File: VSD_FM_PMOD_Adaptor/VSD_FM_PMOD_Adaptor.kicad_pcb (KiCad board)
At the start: 2 copper layers, 58.2 x 29.8 mm, 22 parts, among them J1 PMOD, J2 PMOD, U1 VSDSquadron FM, U2 AMS1117-3.3

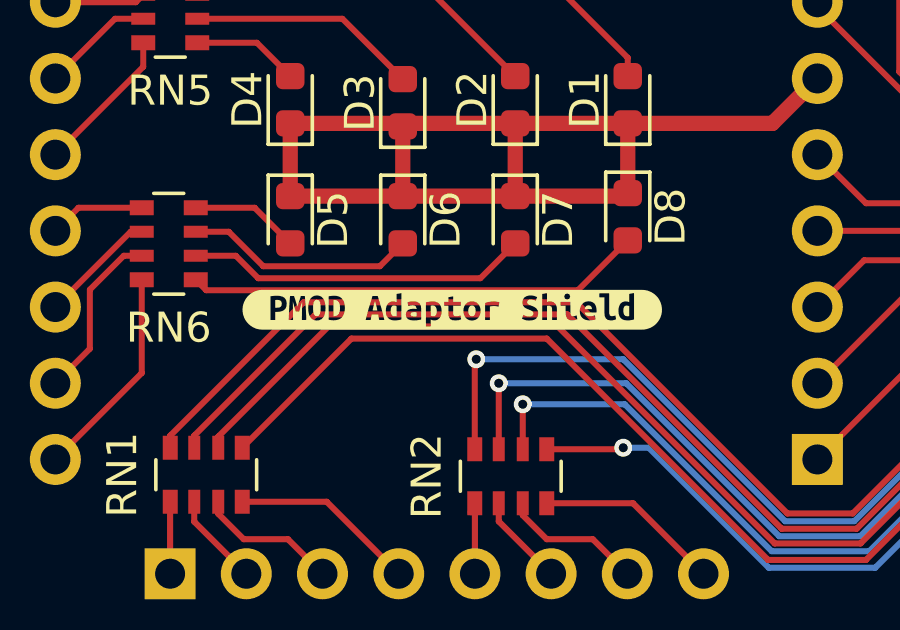
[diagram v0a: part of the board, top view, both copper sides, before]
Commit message: Updated LCSC component part numbers
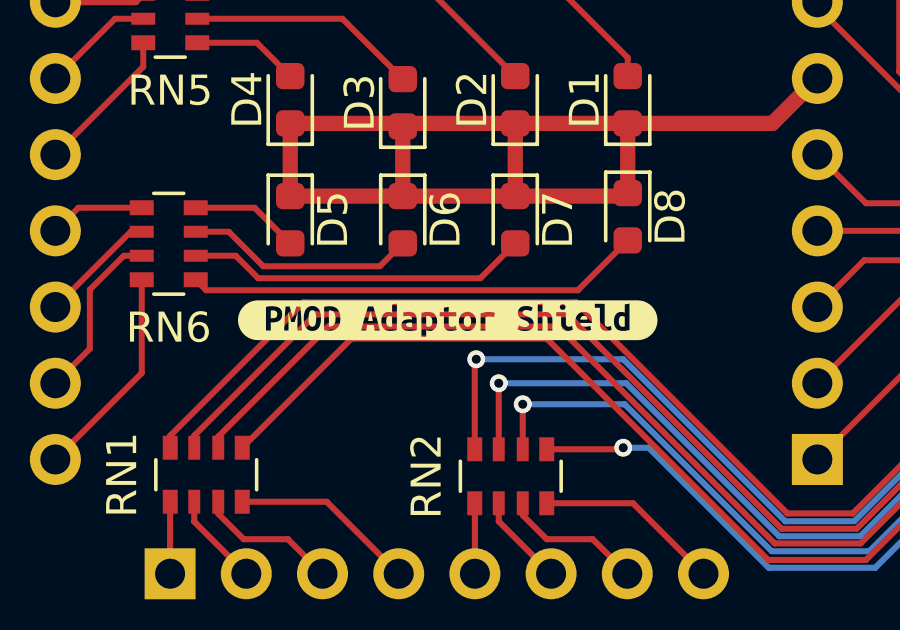
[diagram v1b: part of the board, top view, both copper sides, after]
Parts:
- moved kibuzzard-679249C3 0.38 mm to (126.2, 110.5)
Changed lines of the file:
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@@
 			)
 		)
-		(property "LCSC" ""
+		(property "LCSC" "C965799"
 			(at 0 0 -90)
 			(unlocked yes)
@@
 		(property ki_fp_filters "LED* LED_SMD:* LED_THT:*")
 		(sheetname "Root")
-		(sheetfile "VSD_FM_multi_pmod.kicad_sch")
+		(sheetfile "VSD_FM_PMOD_Adaptor.kicad_sch")
 		(attr smd)
 		(fp_line
@@
 			)
 		)
-		(property "LCSC" ""
+		(property "LCSC" "C965799"
 			(at 0 0 90)
 			(unlocked yes)
@@
 		(property ki_fp_filters "LED* LED_SMD:* LED_THT:*")
 		(sheetname "Root")
-		(sheetfile "VSD_FM_multi_pmod.kicad_sch")
+		(sheetfile "VSD_FM_PMOD_Adaptor.kicad_sch")
 		(attr smd)
 		(fp_line
@@
 	(footprint "kibuzzard-679249C3"
 		(layer "F.Cu")
-		(at 126.4 110.1)
+		(at 126.25 110.45)
 		(descr "Generated with KiBuzzard")
 		(tags "kb_params=eyJBbGlnbm1lbnRDaG9pY2UiOiAiQ2VudGVyIiwgIkNhcExlZnRDaG9pY2UiOiAiKCIsICJDYXBSaWdodENob2ljZSI6ICIpIiwgIkZvbnRDb21ib0JveCI6ICJVYnVudHVNb25vLUIiLCAiSGVpZ2h0Q3RybCI6IDAuOCwgIkxheWVyQ29tYm9Cb3giOiAiRi5TaWxrUyIsICJMaW5lU3BhY2luZ0N0cmwiOiAxLjUsICJNdWx0aUxpbmVUZXh0IjogIlBNT0QgQWRhcHRvciBTaGllbGQiLCAiUGFkZGluZ0JvdHRvbUN0cmwiOiAxLjAsICJQYWRkaW5nTGVmdEN0cmwiOiAyLjUsICJQYWRkaW5nUmlnaHRDdHJsIjogMi41LCAiUGFkZGluZ1RvcEN0cmwiOiAxLjAsICJXaWR0aEN0cmwiOiAwLjAsICJhZHZhbmNlZENoZWNrYm94IjogZmFsc2UsICJpbmxpbmVGb3JtYXRUZXh0Ym94IjogZmFsc2UsICJsaW5lb3ZlclN0eWxlQ2hvaWNlIjogIlNxdWFyZSIsICJsaW5lb3ZlclRoaWNrbmVzc0N0cmwiOiAxfQ==")
@@
 				(font
 					(size 0.001 0.001)
+					(thickness 0.15)
 				)
 			)
@@
 				(font
 					(size 0.001 0.001)
+					(thickness 0.15)
 				)
 			)
@@
 			)
 		)
-		(property "LCSC" ""
+		(property "LCSC" "C6332196"
 			(at 0 0 90)
 			(unlocked yes)
@@
 		(property ki_fp_filters "DIP* SOIC* R*Array*Concave* R*Array*Convex* MSOP*")
 		(sheetname "Root")
-		(sheetfile "VSD_FM_multi_pmod.kicad_sch")
+		(sheetfile "VSD_FM_PMOD_Adaptor.kicad_sch")
 		(attr smd)
 		(fp_line
@@
 			)
 		)
-		(property "LCSC" ""
+		(property "LCSC" "C380337"
 			(at 0 0 0)
 			(unlocked yes)
@@
 		(property ki_fp_filters "C_*")
 		(sheetname "Root")
-		(sheetfile "VSD_FM_multi_pmod.kicad_sch")
+		(sheetfile "VSD_FM_PMOD_Adaptor.kicad_sch")
 		(attr smd)
 		(fp_line
@@
 			)
 		)
-		(property "LCSC" ""
+		(property "LCSC" "C965799"
 			(at 0 0 90)
 			(unlocked yes)
@@
 		(property ki_fp_filters "LED* LED_SMD:* LED_THT:*")
 		(sheetname "Root")
-		(sheetfile "VSD_FM_multi_pmod.kicad_sch")
+		(sheetfile "VSD_FM_PMOD_Adaptor.kicad_sch")
 		(attr smd)
 		(fp_line
@@
 			)
 		)
-		(property "LCSC" ""
+		(property "LCSC" "C172477"
 			(at 0 0 0)
 			(unlocked yes)
@@
 		)
 		(sheetname "Root")
-		(sheetfile "VSD_FM_multi_pmod.kicad_sch")
+		(sheetfile "VSD_FM_PMOD_Adaptor.kicad_sch")
 		(attr smd)
 		(fp_poly
@@
 			)
 		)
-		(property "LCSC" ""
+		(property "LCSC" "C309681"
 			(at 0 0 180)
 			(unlocked yes)
@@
 		(property ki_fp_filters "DIP* SOIC* R*Array*Concave* R*Array*Convex* MSOP*")
 		(sheetname "Root")
-		(sheetfile "VSD_FM_multi_pmod.kicad_sch")
+		(sheetfile "VSD_FM_PMOD_Adaptor.kicad_sch")
 		(attr smd)
 		(fp_line
@@
 			)
 		)
-		(property "LCSC" ""
+		(property "LCSC" "C6332196"
 			(at 0 0 0)
 			(unlocked yes)
@@
 		(property ki_fp_filters "DIP* SOIC* R*Array*Concave* R*Array*Convex* MSOP*")
 		(sheetname "Root")
-		(sheetfile "VSD_FM_multi_pmod.kicad_sch")
+		(sheetfile "VSD_FM_PMOD_Adaptor.kicad_sch")
 		(attr smd)
 		(fp_line
@@
 			)
 		)
-		(property "LCSC" ""
+		(property "LCSC" "C965799"
 			(at 0 0 -90)
 			(unlocked yes)
@@
 		(property ki_fp_filters "LED* LED_SMD:* LED_THT:*")
 		(sheetname "Root")
-		(sheetfile "VSD_FM_multi_pmod.kicad_sch")
+		(sheetfile "VSD_FM_PMOD_Adaptor.kicad_sch")
 		(attr smd)
 		(fp_line
@@
 			)
 		)
-		(property "LCSC" ""
+		(property "LCSC" "C965799"
 			(at 0 0 -90)
 			(unlocked yes)
@@
 		(property ki_fp_filters "LED* LED_SMD:* LED_THT:*")
 		(sheetname "Root")
-		(sheetfile "VSD_FM_multi_pmod.kicad_sch")
+		(sheetfile "VSD_FM_PMOD_Adaptor.kicad_sch")
 		(attr smd)
 		(fp_line
@@
 			)
 		)
-		(property "LCSC" ""
+		(property "LCSC" "IPCP254F12PB28R"
 			(at 0 0 -90)
 			(unlocked yes)
@@
 		(property ki_fp_filters "Connector*:*_2x??_*")
 		(sheetname "Root")
-		(sheetfile "VSD_FM_multi_pmod.kicad_sch")
+		(sheetfile "VSD_FM_PMOD_Adaptor.kicad_sch")
 		(attr through_hole)
 		(fp_line
@@
 			)
 		)
-		(property "LCSC" ""
+		(property "LCSC" "C1713"
 			(at 0 0 0)
 			(unlocked yes)
@@
 		(property ki_fp_filters "C_*")
 		(sheetname "Root")
-		(sheetfile "VSD_FM_multi_pmod.kicad_sch")
+		(sheetfile "VSD_FM_PMOD_Adaptor.kicad_sch")
 		(attr smd)
 		(fp_line
@@
 			)
 		)
-		(property "LCSC" ""
+		(property "LCSC" "C965799"
 			(at 0 0 -90)
 			(unlocked yes)
@@
 		(property ki_fp_filters "Connector*:*_1x??_*")
 		(sheetname "Root")
-		(sheetfile "VSD_FM_multi_pmod.kicad_sch")
+		(sheetfile "VSD_FM_PMOD_Adaptor.kicad_sch")
 		(attr through_hole)
 		(fp_line
@@
 			)
 		)
-		(property "LCSC" ""
+		(property "LCSC" "C965799"
 			(at 0 0 90)
 			(unlocked yes)
@@
 		(property ki_fp_filters "LED* LED_SMD:* LED_THT:*")
 		(sheetname "Root")
-		(sheetfile "VSD_FM_multi_pmod.kicad_sch")
+		(sheetfile "VSD_FM_PMOD_Adaptor.kicad_sch")
 		(attr smd)
 		(fp_line
@@
 			)
 		)
-		(property "LCSC" ""
+		(property "LCSC" "IPCP254F12PB28R"
 			(at 0 0 0)
 			(unlocked yes)
@@
 		(property ki_fp_filters "Connector*:*_2x??_*")
 		(sheetname "Root")
-		(sheetfile "VSD_FM_multi_pmod.kicad_sch")
+		(sheetfile "VSD_FM_PMOD_Adaptor.kicad_sch")
 		(attr through_hole)
 		(fp_line
@@
 			)
 		)
-		(property "LCSC" ""
+		(property "LCSC" "C309681"
 			(at 0 0 180)
 			(unlocked yes)
@@
 		(property ki_fp_filters "DIP* SOIC* R*Array*Concave* R*Array*Convex* MSOP*")
 		(sheetname "Root")
-		(sheetfile "VSD_FM_multi_pmod.kicad_sch")
+		(sheetfile "VSD_FM_PMOD_Adaptor.kicad_sch")
 		(attr smd)
 		(fp_line
@@
 			)
 		)
-		(property "LCSC" ""
+		(property "LCSC" "C6332196"
 			(at 0 0 90)
 			(unlocked yes)
@@
 		(property ki_fp_filters "DIP* SOIC* R*Array*Concave* R*Array*Convex* MSOP*")
 		(sheetname "Root")
-		(sheetfile "VSD_FM_multi_pmod.kicad_sch")
+		(sheetfile "VSD_FM_PMOD_Adaptor.kicad_sch")
 		(attr smd)
 		(fp_line
@@
 			)
 		)
-		(property "LCSC" ""
+		(property "LCSC" "C6332196"
 			(at 0 0 0)
 			(unlocked yes)
@@
 		(property ki_fp_filters "DIP* SOIC* R*Array*Concave* R*Array*Convex* MSOP*")
 		(sheetname "Root")
-		(sheetfile "VSD_FM_multi_pmod.kicad_sch")
+		(sheetfile "VSD_FM_PMOD_Adaptor.kicad_sch")
 		(attr smd)
 		(fp_line
@@
 			)
 		)
-		(property "LCSC" ""
+		(property "LCSC" "C965799"
 			(at 0 0 90)
 			(unlocked yes)
@@
 		(property ki_fp_filters "LED* LED_SMD:* LED_THT:*")
 		(sheetname "Root")
-		(sheetfile "VSD_FM_multi_pmod.kicad_sch")
+		(sheetfile "VSD_FM_PMOD_Adaptor.kicad_sch")
 		(attr smd)
 		(fp_line
@@
 		(property ki_fp_filters "SOT?223*TabPin2*")
 		(sheetname "Root")
-		(sheetfile "VSD_FM_multi_pmod.kicad_sch")
+		(sheetfile "VSD_FM_PMOD_Adaptor.kicad_sch")
 		(attr smd)
 		(fp_line
@@
 			)
 		)
-		(property "LCSC" ""
+		(property "LCSC" "C965799"
 			(at 0 0 -90)
 			(unlocked yes)
@@
 		(property ki_fp_filters "LED* LED_SMD:* LED_THT:*")
 		(sheetname "Root")
-		(sheetfile "VSD_FM_multi_pmod.kicad_sch")
+		(sheetfile "VSD_FM_PMOD_Adaptor.kicad_sch")
 		(attr smd)
 		(fp_line

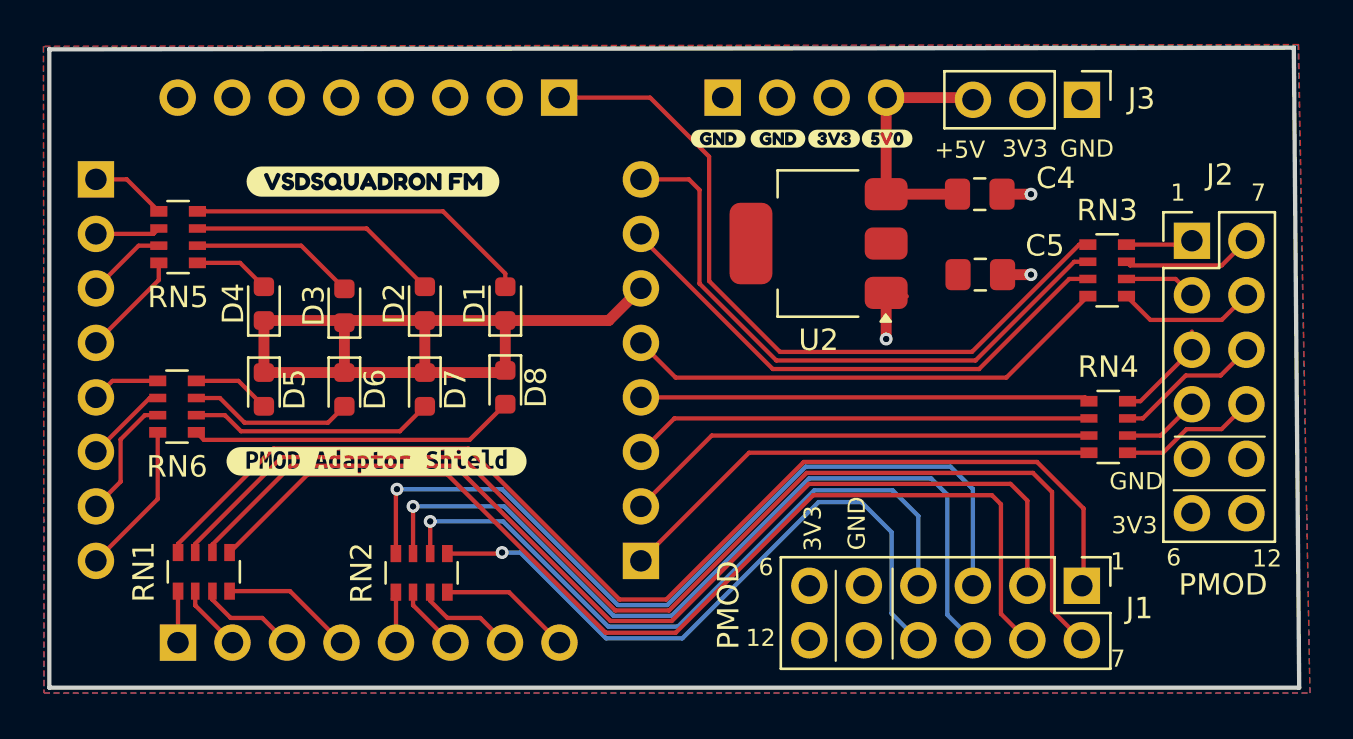
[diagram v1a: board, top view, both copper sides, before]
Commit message: Updated LCSC parts
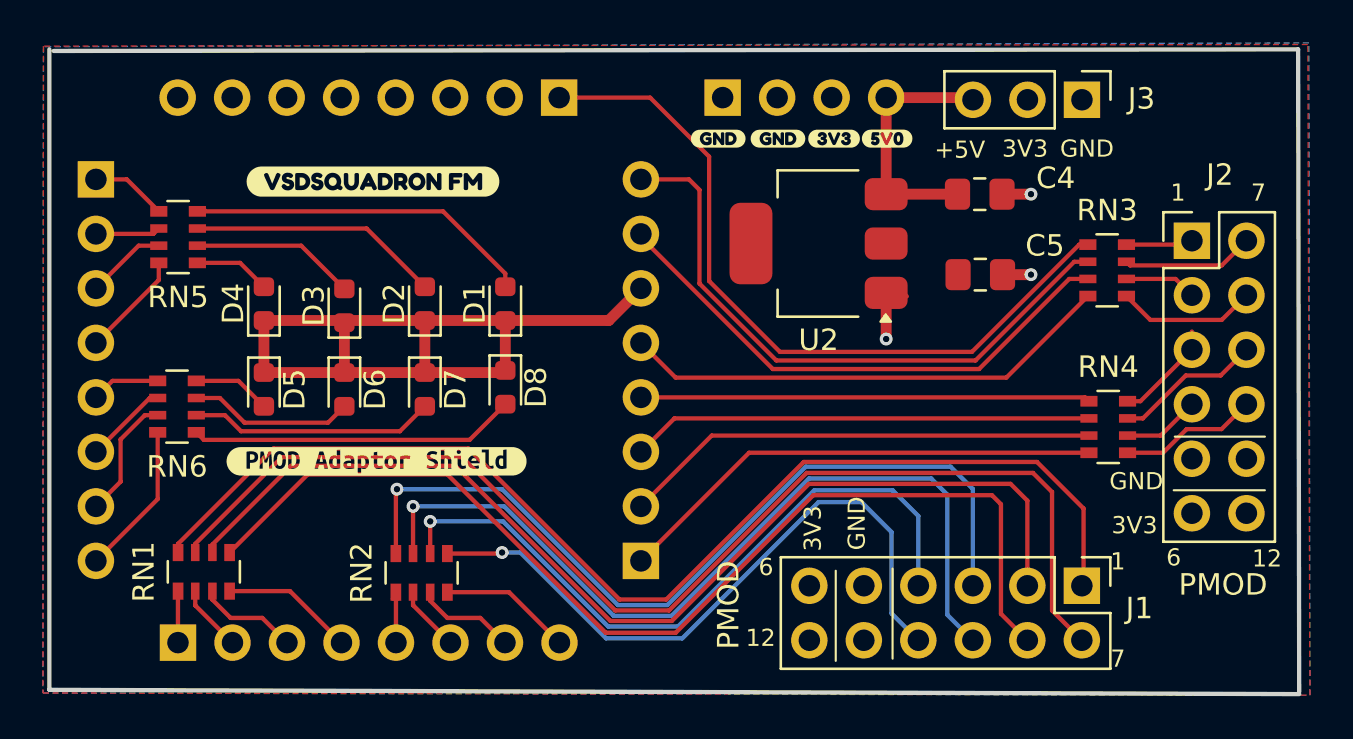
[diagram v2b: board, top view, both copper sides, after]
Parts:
- J3: value ~ -> Shield PWR
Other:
- board size 58.2 x 29.8 mm -> 58.2 x 30 mm
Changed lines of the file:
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@@
 			)
 		)
-		(property "LCSC" "C6332196"
+		(property "LCSC" "C309681"
 			(at 0 0 90)
 			(unlocked yes)
@@
 			)
 		)
-		(property "LCSC" "C172477"
+		(property "LCSC" ""
 			(at 0 0 0)
 			(unlocked yes)
@@
 			)
 		)
-		(property "LCSC" "C309681"
+		(property "LCSC" "C172477"
 			(at 0 0 180)
 			(unlocked yes)
@@
 			)
 		)
-		(property "LCSC" "C6332196"
+		(property "LCSC" "C309681"
 			(at 0 0 0)
 			(unlocked yes)
@@
 			)
 		)
-		(property "LCSC" "IPCP254F12PB28R"
+		(property "LCSC" "C22438455"
 			(at 0 0 -90)
 			(unlocked yes)
@@
 			)
 		)
-		(property "Value" "~"
+		(property "Value" "Shield PWR"
 			(at 0 7.41 90)
 			(layer "F.Fab")
+			(hide yes)
 			(effects
 				(font
@@
 			)
 		)
-		(property "LCSC" "C965799"
+		(property "LCSC" "C6332196"
 			(at 0 0 -90)
 			(unlocked yes)
@@
 			)
 		)
-		(property "LCSC" "IPCP254F12PB28R"
+		(property "LCSC" "C22438455"
 			(at 0 0 0)
 			(unlocked yes)
@@
 			)
 		)
-		(property "LCSC" "C309681"
+		(property "LCSC" "C172477"
 			(at 0 0 180)
 			(unlocked yes)
@@
 			)
 		)
-		(property "LCSC" "C6332196"
+		(property "LCSC" "C309681"
 			(at 0 0 90)
 			(unlocked yes)
@@
 			)
 		)
-		(property "LCSC" "C6332196"
+		(property "LCSC" "C309681"
 			(at 0 0 0)
 			(unlocked yes)
@@
 	)
 	(gr_line
-		(start 111 121)
+		(start 111 121.1)
 		(end 111 91.25)
 		(stroke
@@
 	)
 	(gr_line
-		(start 169.25 121)
-		(end 111 121)
+		(start 169.25 121.3)
+		(end 111 121.1)
 		(stroke
 			(width 0.2)
@@
 	)
 	(gr_line
-		(start 111 91.25)
-		(end 169 91.175)
+		(start 111.2 91.325)
+		(end 169.2 91.25)
 		(stroke
 			(width 0.2)
@@
 	)
 	(gr_line
-		(start 169 91.175)
-		(end 169.25 121)
+		(start 169.2 91.25)
+		(end 169.25 121.2)
 		(stroke
 			(width 0.2)
@@
 		(polygon
 			(pts
-				(xy 110.725 91.1) (xy 110.75 121.25) (xy 169.75 121.25) (xy 169.225 91.025)
+				(xy 110.725 91.1) (xy 110.7 121.25) (xy 169.75 121.35) (xy 169.65 91.025)
 			)
 		)
@@
 		(polygon
 			(pts
-				(xy 110.725 91.125) (xy 110.75 121.25) (xy 169.75 121.25) (xy 169.2 91.05)
+				(xy 110.725 91.125) (xy 110.7 121.25) (xy 169.75 121.35) (xy 169.7 90.95)
 			)
 		)

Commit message: Adjust fill zones a bit
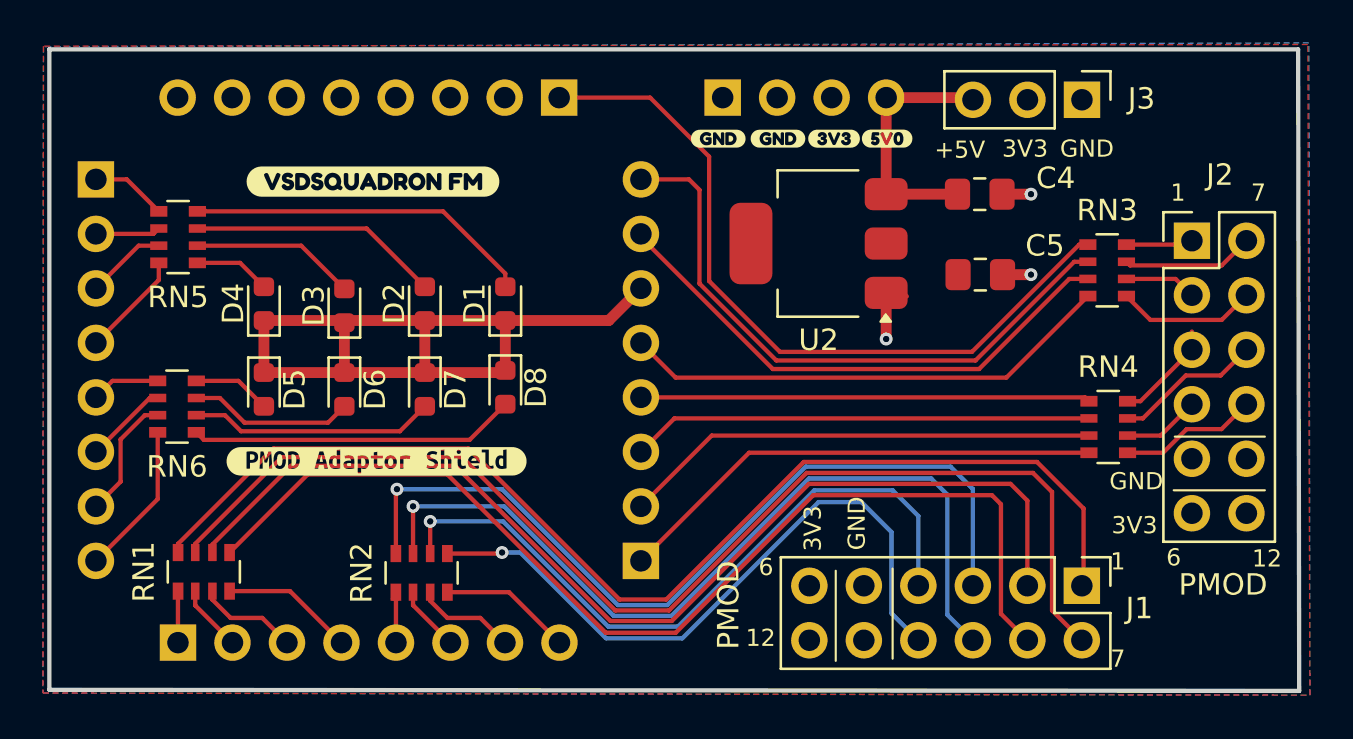
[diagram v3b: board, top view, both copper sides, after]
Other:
- board size 58.2 x 30 mm -> 58.2 x 29.9 mm
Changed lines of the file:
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@@
 	)
 	(paper "A4")
+	(title_block
+		(title "PMOD Adaptor for VSDSquadron FM Shield")
+		(date "2025-01-25")
+		(rev "1A")
+		(company "David Brough-Smyth")
+	)
 	(layers
 		(0 "F.Cu" signal)
@@
 	)
 	(gr_line
-		(start 169.25 121.3)
+		(start 169.25 121.15)
 		(end 111 121.1)
 		(stroke
@@
 	)
 	(gr_line
-		(start 111.2 91.325)
+		(start 111 91.25)
 		(end 169.2 91.25)
 		(stroke
@@
 	(gr_line
 		(start 169.2 91.25)
-		(end 169.25 121.2)
+		(end 169.25 121.15)
 		(stroke
 			(width 0.2)
